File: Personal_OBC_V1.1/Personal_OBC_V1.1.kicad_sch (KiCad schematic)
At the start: 4 parts, among them U1 STM32F302K8Ux, U2 MS560702BA03-50, X1 ECS-2520MV-xxx-xx

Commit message: p
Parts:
- added C2: 0.1uF, Capacitor_SMD:C_0402_1005Metric, symbol Device:C
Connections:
- net GND: now also C2.1
- net BOOT0: now reaches U1.31 (BOOT0)
- net at U1.4 (NRST): now also C2.2
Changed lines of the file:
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@@
+    (stroke (width 0) (type default))
+  )
+  (wire (pts (xy 29.21 29.21) (xy 32.385 29.21))
     (stroke (width 0) (type default))
   )
@@
     (stroke (width 0) (type default))
   )
+  (wire (pts (xy 21.59 29.21) (xy 15.24 29.21))
+    (stroke (width 0) (type default))
+  )
   (wire (pts (xy 280.67 20.32) (xy 280.67 24.13))
     (stroke (width 0) (type default))
@@
     (stroke (width 0) (type default))
   )
+  (wire (pts (xy 30.48 34.29) (xy 32.385 34.29))
+    (stroke (width 0) (type default))
+  )
+  (wire (pts (xy 15.24 29.21) (xy 15.24 32.385))
+    (stroke (width 0) (type default))
+  )
   (wire (pts (xy 45.085 76.2) (xy 45.085 77.47))
     (stroke (width 0) (type default))
@@
     (property "Intersheetrefs" "${INTERSHEET_REFS}" (at 72.5328 59.69 0)
       (effects (font (size 1.27 1.27)) (justify left) hide)
+    )
+  )
+  (global_label "BOOT0" (shape input) (at 30.48 34.29 180) (fields_autoplaced)
+    (effects (font (size 1.27 1.27)) (justify right))
+    (property "Intersheetrefs" "${INTERSHEET_REFS}" (at 21.3867 34.29 0)
+      (effects (font (size 1.27 1.27)) (justify right) hide)
     )
   )
@@
     )
   )
+  (symbol (lib_id "power:GND") (at 15.24 32.385 0) (unit 1)
+    (in_bom yes) (on_board yes) (dnp no) (fields_autoplaced)
+    (property "Reference" "#PWR06" (at 15.24 38.735 0)
+      (effects (font (size 1.27 1.27)) hide)
+    )
+    (property "Value" "GND" (at 15.24 37.465 0)
+      (effects (font (size 1.27 1.27)) hide)
+    )
+    (property "Footprint" "" (at 15.24 32.385 0)
+      (effects (font (size 1.27 1.27)) hide)
+    )
+    (property "Datasheet" "" (at 15.24 32.385 0)
+      (effects (font (size 1.27 1.27)) hide)
+    )
+    (pin "1")
+    (instances
+      (project "Personal_OBC_V1.1"
+        (path "/7aafcae6-20fd-4029-823b-72b16b42b1cc"
+          (reference "#PWR06") (unit 1)
+        )
+      )
+    )
+  )
   (symbol (lib_id "power:+3.3V") (at 45.085 20.32 0) (unit 1)
     (in_bom yes) (on_board yes) (dnp no) (fields_autoplaced)
@@
         )
       )
+    )
+  )
+  (symbol (lib_id "Device:C") (at 25.4 29.21 90) (unit 1)
+    (in_bom yes) (on_board yes) (dnp no)
+    (property "Reference" "C2" (at 25.4 26.035 90)
+      (effects (font (size 1.27 1.27)))
+    )
+    (property "Value" "0.1uF" (at 29.21 27.94 90)
+      (effects (font (size 1.27 1.27)))
+    )
+    (property "Footprint" "Capacitor_SMD:C_0402_1005Metric" (at 29.21 28.2448 0)
+      (effects (font (size 1.27 1.27)) hide)
+    )
+    (property "Datasheet" "~" (at 25.4 29.21 0)
+      (effects (font (size 1.27 1.27)) hide)
+    )
+    (pin "1")
+    (pin "2")
+    (instances
+      (project "Personal_OBC_V1.1"
+        (path "/7aafcae6-20fd-4029-823b-72b16b42b1cc"
+          (reference "C2") (unit 1)
+        )
+      )

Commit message: A
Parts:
- added U3: W25X40CLUXIG_TR, W25X40CLUXIG_TR:PSON50P300X200X60-9N, symbol W25X40CLUXIG TR:W25X40CLUXIG_TR
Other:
- moved on the sheet: X1
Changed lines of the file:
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@@
     )
   )
-  (symbol (lib_id "Oscillator:ECS-2520MV-xxx-xx") (at 99.06 99.695 0) (unit 1)
-    (in_bom yes) (on_board yes) (dnp no) (fields_autoplaced)
-    (property "Reference" "X1" (at 118.11 96.0471 0)
-      (effects (font (size 1.27 1.27)))
-    )
-    (property "Value" "ECS-2520MV-xxx-xx" (at 118.11 98.5871 0)
-      (effects (font (size 1.27 1.27)))
-    )
-    (property "Footprint" "Oscillator:Oscillator_SMD_ECS_2520MV-xxx-xx-4Pin_2.5x2.0mm" (at 110.49 108.585 0)
-      (effects (font (size 1.27 1.27)) hide)
-    )
-    (property "Datasheet" "https://www.ecsxtal.com/store/pdf/ECS-2520MV.pdf" (at 94.615 96.52 0)
+  (symbol (lib_id "Oscillator:ECS-2520MV-xxx-xx") (at 39.37 110.49 0) (unit 1)
+    (in_bom yes) (on_board yes) (dnp no) (fields_autoplaced)
+    (property "Reference" "X1" (at 58.42 106.8421 0)
+      (effects (font (size 1.27 1.27)))
+    )
+    (property "Value" "ECS-2520MV-xxx-xx" (at 58.42 109.3821 0)
+      (effects (font (size 1.27 1.27)))
+    )
+    (property "Footprint" "Oscillator:Oscillator_SMD_ECS_2520MV-xxx-xx-4Pin_2.5x2.0mm" (at 50.8 119.38 0)
+      (effects (font (size 1.27 1.27)) hide)
+    )
+    (property "Datasheet" "https://www.ecsxtal.com/store/pdf/ECS-2520MV.pdf" (at 34.925 107.315 0)
       (effects (font (size 1.27 1.27)) hide)
     )
@@
         )
       )
+    )
+  )
+  (symbol (lib_id "W25X40CLUXIG TR:W25X40CLUXIG_TR") (at 180.34 39.37 0) (unit 1)
+    (in_bom yes) (on_board yes) (dnp no) (fields_autoplaced)
+    (property "Reference" "U3" (at 180.34 16.51 0)
+      (effects (font (size 1.27 1.27)))
+    )
+    (property "Value" "W25X40CLUXIG_TR" (at 180.34 19.05 0)
+      (effects (font (size 1.27 1.27)))
+    )
+    (property "Footprint" "W25X40CLUXIG_TR:PSON50P300X200X60-9N" (at 180.34 39.37 0)
+      (effects (font (size 1.27 1.27)) (justify bottom) hide)
+    )
+    (property "Datasheet" "" (at 180.34 39.37 0)
+      (effects (font (size 1.27 1.27)) hide)
+    )
+    (property "MF" "Winbond Electronics" (at 180.34 39.37 0)
+      (effects (font (size 1.27 1.27)) (justify bottom) hide)
+    )
+    (property "Description" "\nFLASH Memory IC 4Mb (512K x 8) SPI 104 MHz 8-USON (2x3)\n" (at 180.34 39.37 0)
+      (effects (font (size 1.27 1.27)) (justify bottom) hide)
+    )
+    (property "Package" "UFDFN-8 Winbond" (at 180.34 39.37 0)
+      (effects (font (size 1.27 1.27)) (justify bottom) hide)
+    )
+    (property "Price" "None" (at 180.34 39.37 0)
+      (effects (font (size 1.27 1.27)) (justify bottom) hide)
+    )
+    (property "Check_prices" "https://www.snapeda.com/parts/W25X40CLUXIG%20TR/Winbond+Electronics/view-part/?ref=eda" (at 180.34 39.37 0)
+      (effects (font (size 1.27 1.27)) (justify bottom) hide)
+    )
+    (property "STANDARD" "IPC-7351B" (at 180.34 39.37 0)
+      (effects (font (size 1.27 1.27)) (justify bottom) hide)
+    )
+    (property "PARTREV" "F" (at 180.34 39.37 0)
+      (effects (font (size 1.27 1.27)) (justify bottom) hide)
+    )
+    (property "SnapEDA_Link" "https://www.snapeda.com/parts/W25X40CLUXIG%20TR/Winbond+Electronics/view-part/?ref=snap" (at 180.34 39.37 0)
+      (effects (font (size 1.27 1.27)) (justify bottom) hide)
+    )
+    (property "MP" "W25X40CLUXIG TR" (at 180.34 39.37 0)
+      (effects (font (size 1.27 1.27)) (justify bottom) hide)
+    )
+    (property "Purchase-URL" "https://www.snapeda.com/api/url_track_click_mouser/?unipart_id=424425&manufacturer=Winbond Electronics&part_name=W25X40CLUXIG TR&search_term=None" (at 180.34 39.37 0)
+      (effects (font (size 1.27 1.27)) (justify bottom) hide)
+    )
+    (property "Availability" "In Stock" (at 180.34 39.37 0)
+      (effects (font (size 1.27 1.27)) (justify bottom) hide)
+    )
+    (property "MANUFACTURER" "Winbond" (at 180.34 39.37 0)
+      (effects (font (size 1.27 1.27)) (justify bottom) hide)
+    )
+    (pin "1")
+    (pin "2")
+    (pin "3")
+    (pin "4")
+    (pin "5")
+    (pin "6")
+    (pin "7")
+    (pin "8")
+    (pin "9")
+    (instances
+      (project "Personal_OBC_V1.1"
+        (path "/7aafcae6-20fd-4029-823b-72b16b42b1cc"
+          (reference "U3") (unit 1)
+        )
+      )

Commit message: Personal Work
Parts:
- added C10: 10nF, Capacitor_SMD:C_0402_1005Metric, symbol Device:C
- added C11: 1uF, Capacitor_SMD:C_0402_1005Metric, symbol Device:C
- added C4, C8: 20pF, Capacitor_SMD:C_0402_1005Metric, symbol Device:C
- added C5, C6, C7, C8: 100nF, Capacitor_SMD:C_0402_1005Metric, symbol Device:C
- added C9: 4.7uF, Capacitor_SMD:C_0402_1005Metric, symbol Device:C
- added H1 (x2), H2 (x2): MountingHole_Pad, MountingHole:MountingHole_3.2mm_M3_Pad_TopBottom, symbol Mechanical:MountingHole_Pad
- added J4: Conn_01x04_Socket, Connector_PinHeader_2.54mm:PinHeader_1x04_P2.54mm_Vertical, symbol Connector:Conn_01x04_Socket
- added R1: 10k, Resistor_SMD:R_0402_1005Metric, symbol Device:R
- added SW1: SW_SPDT, Jumper:SolderJumper-3_P1.3mm_Open_RoundedPad1.0x1.5mm_NumberLabels, symbol Switch:SW_SPDT
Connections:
- net +3.3V: now also U3.8 (VCC), C10.1, C11.1, C5.1, C6.1, C7.1, C8.1, C9.1, J4.3 (Pin_3), SW1.3 (C)
- net BOOT0: now also R1.1
- net GND: now also U3.4 (GND), U3.9 (EXP), X1.2 (GND), X1.4 (VDD), C10.2, C11.2, C4.2, C5.2, C6.2, C7.2, C8.2, C8.2, C9.2, H1.1, H1.1, H2.1, H2.1, J4.4 (Pin_4), SW1.1 (A)
- net SYS_SWCLK: now also J4.2 (Pin_2)
- net SYS_SWDIO: now also J4.1 (Pin_1)
- net RCC_OSC_IN: now reaches X1.1 (Tri-State)
- net RCC_OSC_IN: now also C4.1
- net RCC_OSC_OUT: now reaches X1.3 (OUT)
- net RCC_OSC_OUT: now also C8.1
- new net: R1.2, SW1.2 (B)
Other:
- note added: "Baro Alt: MS5607"
- note added: "Crystal Oscillator"
- note added: "Decoupling Caps"
- note added: "Flash Chip: W25Q01JVZEIQ"
- note added: "MPU: STM32F302K8U6"
- note added: "Mounting Holes"
- note added: "Prog Pins"
- note added: "Run/Debug"
- note added: "VDD"
- note added: "VDDA"
- moved on the sheet: C1, U2, U3, X1

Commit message: Personal Altimeter
Needs Radio Part
Needs Pyro Channels
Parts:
- added C12, C13: 1.0uF, symbol Device:C
- added IC1: AP2205-33W5-7, AP2205-33W5-7:SOT95P282X130-5N, symbol AP2205-33W5-7:AP2205-33W5-7
- added J2: PYRO CHANNELS, symbol Connector:Screw_Terminal_01x04
- added J3: POWER IN, symbol Connector:Screw_Terminal_01x04
- added J4: USB_B_Micro, Connector_USB:USB_Micro-B_Amphenol_10104110_Horizontal, symbol Connector:USB_B_Micro
- added R2: 5.6k, symbol Device:R
- added R3: 10k, symbol Device:R
- J4: value Conn_01x04_Socket -> PROG PINS
- U2: footprint MS5607:SON125P300X500X100-8N -> MS560702BA03-50:SON125P300X500X100-8N
- U3: footprint W25X40CLUXIG_TR:PSON50P300X200X60-9N -> W25X40CLUXIG TR:PSON50P300X200X60-9N
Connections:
- net +3.3V: now also U3.3 (~{WP}), U3.7 (~{HOLD}), C13.1, IC1.5 (VOUT)
- net GND: now also C12.2, C13.2, IC1.2 (GND), J3.4 (Pin_4), J4.5 (GND), J4.6 (Shield), R3.2
- net MISO: now also U3.2 (DO(IO1))
- net MOSI: now also U3.5 (DI(IO0))
- net SCLK: now also U3.6 (CLK)
- net USB_DM: now also J4.2 (D-)
- net USB_DP: now also J4.3 (D+)
- net CS_MEM: now reaches U1.29 (PB6)
- net CS_MEM: now also U3.1 (~{CS})
- net ENABLE: now reaches U1.7 (PA0)
- net CONFIG: now reaches U1.8 (PA1)
- new net BATT+: J3.2 (Pin_2), J3.3 (Pin_3)
- new net PWR+: C12.1, IC1.1 (VIN), IC1.3 (EN), J3.1 (Pin_1), J4.1 (VBUS), R2.1
- new net V_BAT: R2.2, R3.1
- no-connect marks 0 -> 1
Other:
- note added: "Battery Sensor"
- note added: "Input: 24V Max Output: 3.3V, 250mA"
- note added: "Power Terminals"
- note added: "Spec For 2S LI-PO"
- note added: "USB_B_Micro"
- note added: "Voltage Reg"

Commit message: Reworked schematic
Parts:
- added U4: HM-TRPW, HW-TRPW:HM-TRPW, symbol HW-TRPW:HW-TRPW
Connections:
- net +3.3V: now also U4.1 (VCC)
- net CONFIG: now also U4.5 (CONFIG)
- net ENABLE: now also U4.6 (ENABLE)
- net GND: now also U4.3 (GND), U4.9 (GND)
- net PWR+: now also J2.1 (Pin_1), J2.3 (Pin_3)
- net USART_RX: now also U4.4 (DRX)
- net USART_TX: now also U4.2 (DTX)
- net FET_APOGEE: now reaches J2.2 (Pin_2)
- net FET_MAIN: now reaches J2.4 (Pin_4)
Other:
- note added: "Radio Board: HM-TRPW"
- note added: "Screw Terminals"
- note removed: "Power Terminals"
- moved on the sheet: C12, C13, IC1, J2, J3, R2, R3

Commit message: Sent
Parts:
- added R4, R6: 100k, symbol Device:R
- added R5, R7: 27k, symbol Device:R
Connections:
- net FET_APOGEE: now also R6.1
- net FET_MAIN: now also R4.1
- net GND: now also R5.2, R7.2
- new net SENSE_APOGEE: R6.2, R7.1
- new net SENSE_MAIN: R4.2, R5.1
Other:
- note added: "Apogee"
- note added: "Continuity Check"
- note added: "MOSFETS"
- note added: "Main"

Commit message: Mosfets Required
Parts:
- added D1, D2: LED, symbol Device:LED
- added J5: 636101111001, 636101111001, symbol 636101111001:636101111001
- added R8, R9: FIND, symbol Device:R
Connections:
- net CS_Alt is gone; now on net CS_ALT: U2.4 (~{CSB}), U2.5 (~{CSB})
- net FET_APOGEE: now also R9.1
- net FET_MAIN: now also R8.1
- net GND: now also D1.1 (K), D2.1 (K), J5.1, J5.3
- net TO_ANT: now reaches U4.8 (ANT)
- net TO_ANT: now also J5.2
- new net: D1.2 (A), R8.2
- new net: D2.2 (A), R9.2
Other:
- note added: "Antenna"
- moved on the sheet: J2, J3, R4, R5, R6, R7

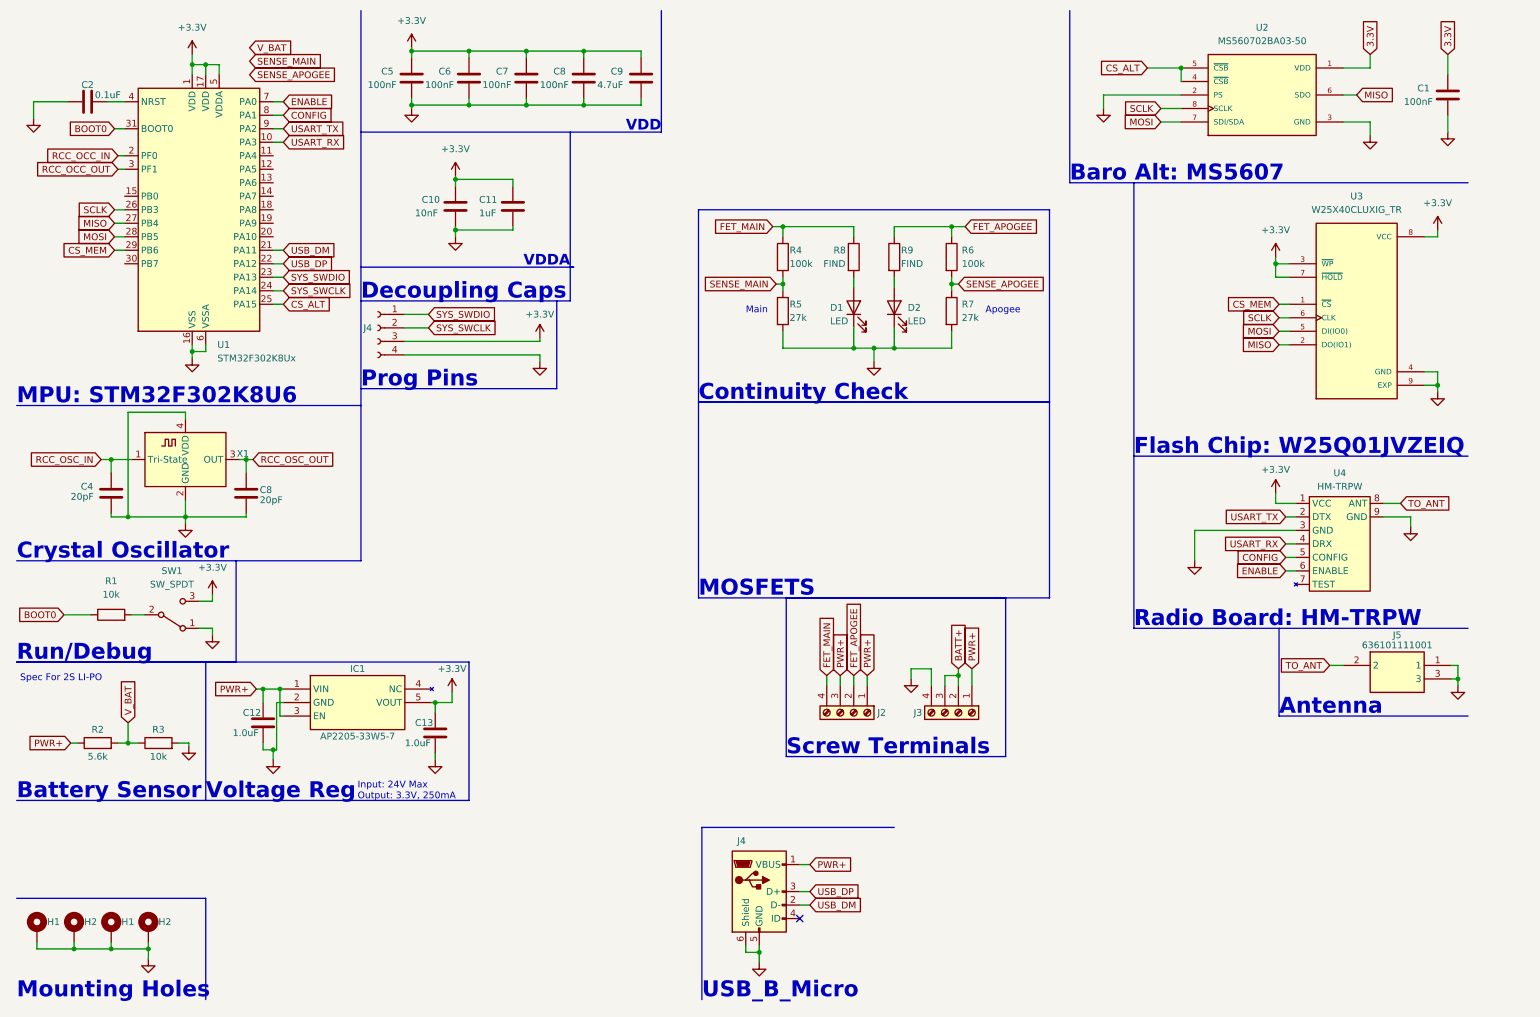
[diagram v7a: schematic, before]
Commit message: Got the mosfets
Needs resistor values
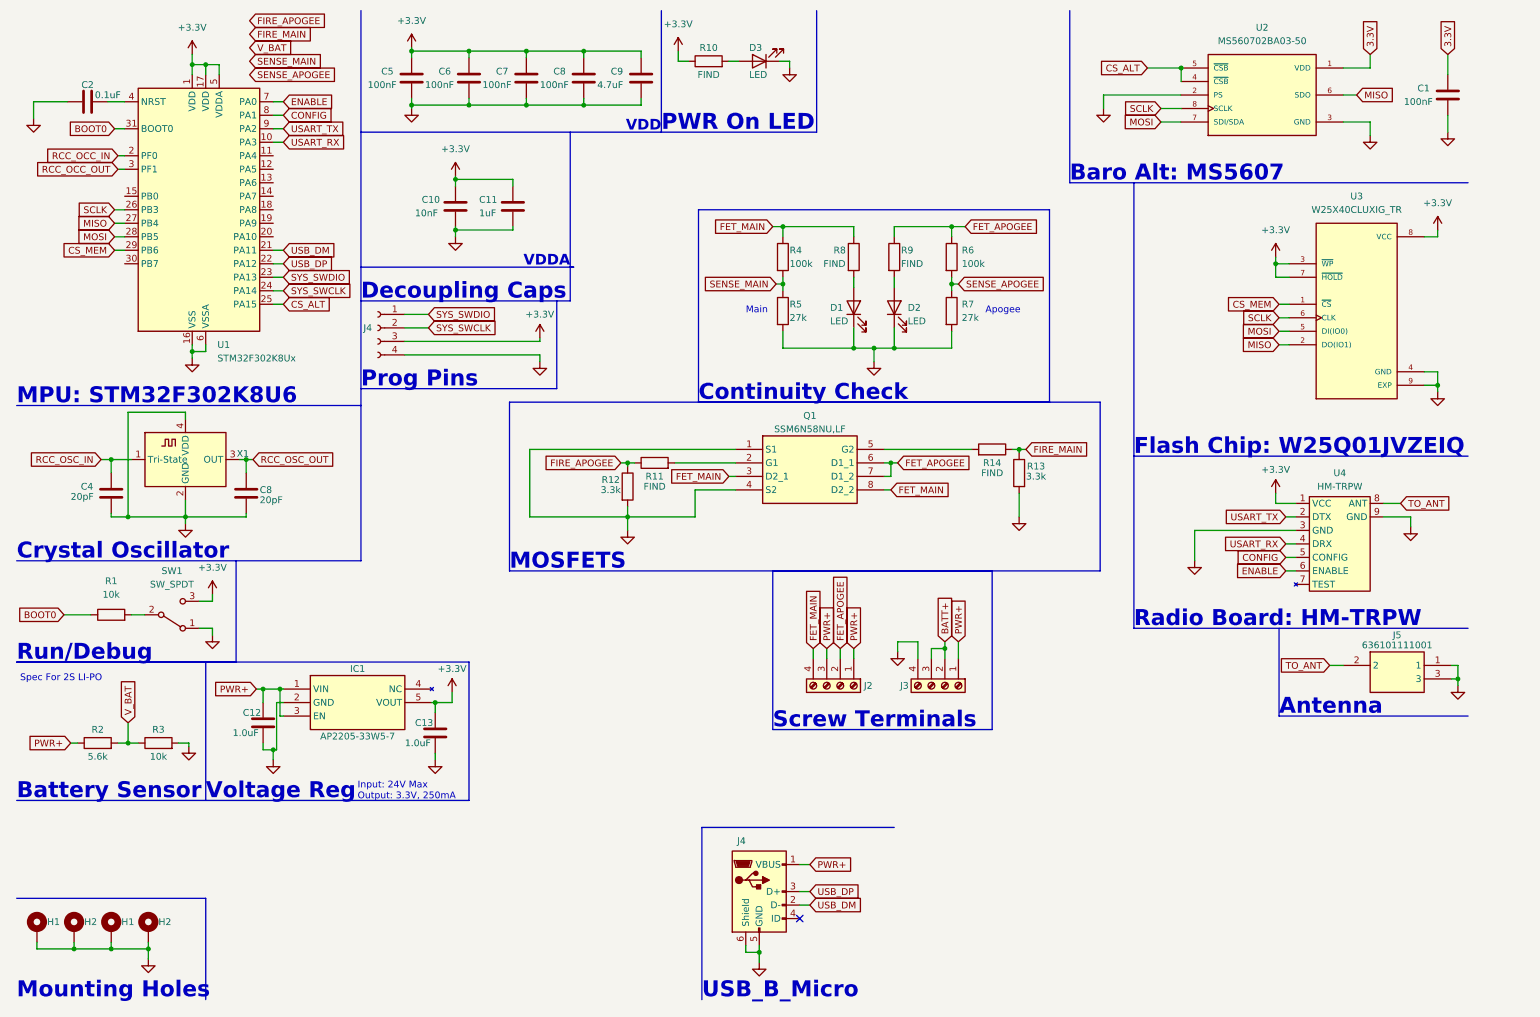
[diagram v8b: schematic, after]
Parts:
- added D3: LED, symbol Device:LED
- added Q1: SSM6N58NU,LF, SSM6N58NULF, symbol SSM6N58NU,LF:SSM6N58NU,LF
- added R10, R11, R14: FIND, symbol Device:R
- added R12, R13: 3.3k, symbol Device:R
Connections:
- net +3.3V: now also R10.1
- net FET_APOGEE: now also Q1.6 (D1_1), Q1.7 (D1_2)
- net FET_MAIN: now also Q1.3 (D2_1), Q1.8 (D2_2)
- net GND: now also D3.1 (K), Q1.1 (S1), Q1.4 (S2), R12.2, R13.2
- new net: Q1.2 (G1), R11.2
- new net: Q1.5 (G2), R14.2
- new net: D3.2 (A), R10.2
- new net FIRE_APOGEE: R11.1, R12.1
- new net FIRE_MAIN: R13.1, R14.1
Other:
- note added: "PWR On LED"
- moved on the sheet: J2, J3
